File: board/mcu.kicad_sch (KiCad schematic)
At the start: 21 parts, among them J2 PinHeader_01x05, J3 TC2030-MCP-NL, SW1 SW_Push, U1 STM32F030C8Tx, U2 SRV05-4, Y1 16Mhz

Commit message: Update schematic
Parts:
- removed D1: Status, symbol Device:LED_Small
- removed R3: 1k, symbol Device:R_Small
- R301: renamed from R2; value 47 -> 10k
- R303: renamed from R502; value 100R -> 150R
- R304: renamed from R501; value 100R -> 150R
- R305: renamed from R504; value 100R -> 150R
- renumbered C8 to C301, C10 to C302, C9 to C303, C4 to C304, C5 to C305, C6 to C306, C7 to C307, C11 to C308, J3 to J301, J2 to J302, R1 to R302, SW1 to SW301, U1 to U301, U2 to U302, Y1 to Y301
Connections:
- net MCU_BOOT0 renamed OPT_BOOT0
- no-connect marks 1 -> 2
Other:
- note removed: "Status Indicators"
- company: (none) -> BlueDot, Vincenzo Fortunato
- title: (none) -> BD845-PWB

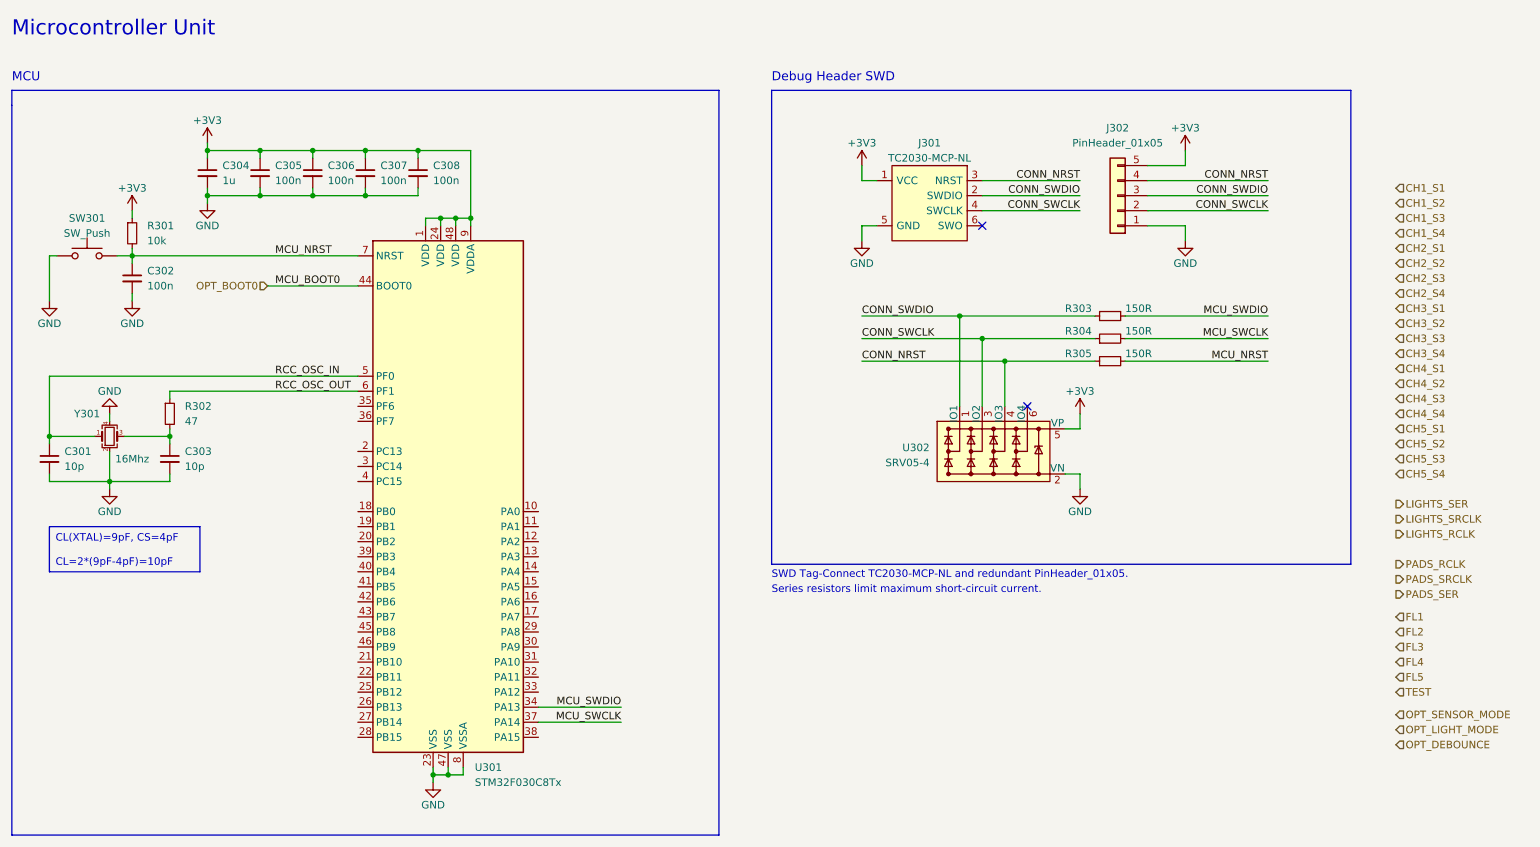
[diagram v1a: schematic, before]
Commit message: Schematic done
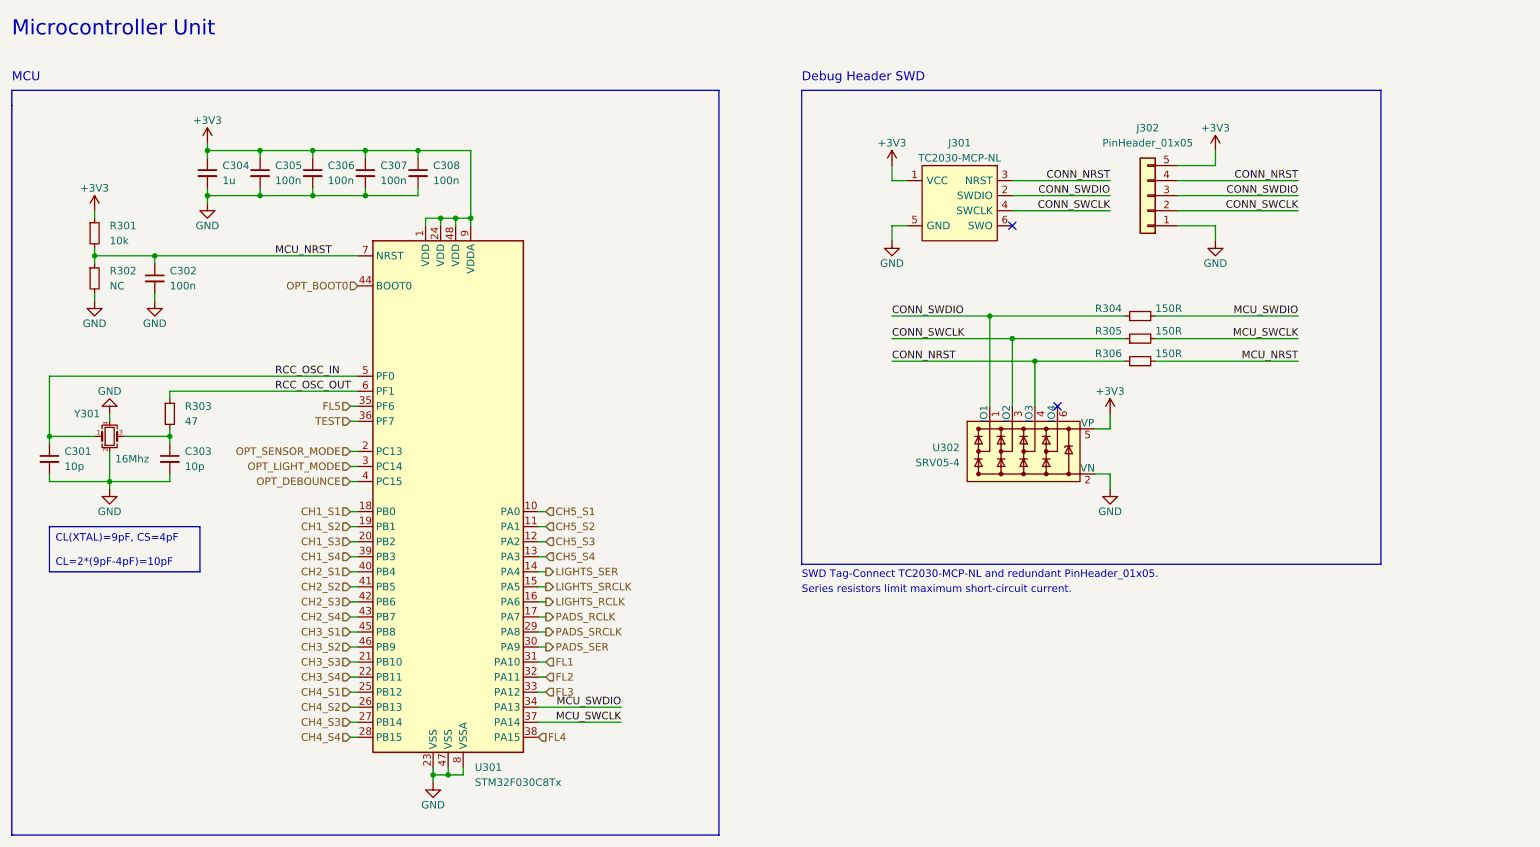
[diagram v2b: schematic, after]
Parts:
- removed SW301: SW_Push, symbol Switch:SW_Push
- added R302: NC, Resistor_SMD:R_0603_1608Metric, symbol Device:R_Small
- C301, C302, C303, C304, C305, C306, C307, C308: footprint (none) -> Capacitor_SMD:C_0603_1608Metric
- J302: footprint (none) -> Connector_PinHeader_2.54mm:PinHeader_1x05_P2.54mm_Vertical
- R301: footprint (none) -> Resistor_SMD:R_0603_1608Metric
- R303: renamed from R302; footprint (none) -> Resistor_SMD:R_0603_1608Metric
- R304: renamed from R303; footprint (none) -> Resistor_SMD:R_0603_1608Metric
- R305: renamed from R304; footprint (none) -> Resistor_SMD:R_0603_1608Metric
- R306: renamed from R305; footprint (none) -> Resistor_SMD:R_0603_1608Metric
- Y301: footprint (none) -> Crystal:Crystal_SMD_3225-4Pin_3.2x2.5mm
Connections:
- net CH1_S1: now also U301.18 (PB0)
- net CH1_S2: now also U301.19 (PB1)
- net CH1_S3: now also U301.20 (PB2)
- net CH1_S4: now also U301.39 (PB3)
- net CH2_S1: now also U301.40 (PB4)
- net CH2_S2: now also U301.41 (PB5)
- net CH2_S3: now also U301.42 (PB6)
- net CH2_S4: now also U301.43 (PB7)
- net CH3_S1: now also U301.45 (PB8)
- net CH3_S2: now also U301.46 (PB9)
- net CH3_S3: now also U301.21 (PB10)
- net CH3_S4: now also U301.22 (PB11)
- net CH4_S1: now also U301.25 (PB12)
- net CH4_S2: now also U301.26 (PB13)
- net CH4_S3: now also U301.27 (PB14)
- net CH4_S4: now also U301.28 (PB15)
- net CH5_S1: now also U301.10 (PA0)
- net CH5_S2: now also U301.11 (PA1)
- net CH5_S3: now also U301.12 (PA2)
- net CH5_S4: now also U301.13 (PA3)
- net FL1: now also U301.31 (PA10)
- net FL2: now also U301.32 (PA11)
- net FL3: now also U301.33 (PA12)
- net FL4: now also U301.38 (PA15)
- net FL5: now also U301.35 (PF6)
- net GND: now also R302.2
- net LIGHTS_RCLK: now also U301.16 (PA6)
- net LIGHTS_SER: now also U301.14 (PA4)
- net LIGHTS_SRCLK: now also U301.15 (PA5)
- net MCU_NRST: now also R302.1
- net OPT_DEBOUNCE: now also U301.4 (PC15)
- net OPT_LIGHT_MODE: now also U301.3 (PC14)
- net OPT_SENSOR_MODE: now also U301.2 (PC13)
- net PADS_RCLK: now also U301.17 (PA7)
- net PADS_SER: now also U301.30 (PA9)
- net PADS_SRCLK: now also U301.29 (PA8)
- net TEST: now also U301.36 (PF7)
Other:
- moved on the sheet: C302, J301, J302, R301, R304, R305, R306, U302

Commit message: Update PCB
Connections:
- net CH1_S1: now also U301.35 (PF6); no longer U301.18 (PB0)
- net CH1_S2: now also U301.33 (PA12); no longer U301.19 (PB1)
- net CH1_S3: now also U301.32 (PA11); no longer U301.20 (PB2)
- net CH1_S4: now also U301.31 (PA10); no longer U301.39 (PB3)
- net CH2_S1: now also U301.30 (PA9); no longer U301.40 (PB4)
- net CH2_S2: now also U301.29 (PA8); no longer U301.41 (PB5)
- net CH2_S3: now also U301.28 (PB15); no longer U301.42 (PB6)
- net CH2_S4: now also U301.27 (PB14); no longer U301.43 (PB7)
- net CH3_S1: now also U301.26 (PB13); no longer U301.45 (PB8)
- net CH3_S2: now also U301.25 (PB12); no longer U301.46 (PB9)
- net CH3_S3: now also U301.22 (PB11); no longer U301.21 (PB10)
- net CH3_S4: now also U301.21 (PB10); no longer U301.22 (PB11)
- net CH4_S1: now also U301.20 (PB2); no longer U301.25 (PB12)
- net CH4_S2: now also U301.19 (PB1); no longer U301.26 (PB13)
- net CH4_S3: now also U301.18 (PB0); no longer U301.27 (PB14)
- net CH4_S4: now also U301.17 (PA7); no longer U301.28 (PB15)
- net CH5_S1: now also U301.16 (PA6); no longer U301.10 (PA0)
- net CH5_S2: now also U301.15 (PA5); no longer U301.11 (PA1)
- net CH5_S3: now also U301.14 (PA4); no longer U301.12 (PA2)
- net FL1: now also U301.46 (PB9); no longer U301.31 (PA10)
- net FL2: now also U301.45 (PB8); no longer U301.32 (PA11)
- net FL3: now also U301.43 (PB7); no longer U301.33 (PA12)
- net FL4: now also U301.42 (PB6); no longer U301.38 (PA15)
- net FL5: now also U301.41 (PB5); no longer U301.35 (PF6)
- net LIGHTS_RCLK: now also U301.11 (PA1); no longer U301.16 (PA6)
- net LIGHTS_SER: now also U301.12 (PA2); no longer U301.14 (PA4)
- net LIGHTS_SRCLK: now also U301.10 (PA0); no longer U301.15 (PA5)
- net OPT_DEBOUNCE: now also U301.38 (PA15); no longer U301.4 (PC15)
- net OPT_LIGHT_MODE: now also U301.36 (PF7); no longer U301.3 (PC14)
- net OPT_SENSOR_MODE: now also U301.39 (PB3); no longer U301.2 (PC13)
- net PADS_RCLK: now also U301.3 (PC14); no longer U301.17 (PA7)
- net PADS_SER: now also U301.2 (PC13); no longer U301.30 (PA9)
- net PADS_SRCLK: now also U301.4 (PC15); no longer U301.29 (PA8)
- net TEST: now also U301.40 (PB4); no longer U301.36 (PF7)

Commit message: Update PCB
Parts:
- C304: value 1u -> 10u
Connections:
- net CONN_NRST: now also R304.1, U302.1 (IO1); no longer R306.1, U302.4 (IO3)
- net CONN_SWDIO: now also R306.1, U302.4 (IO3); no longer R304.1, U302.1 (IO1)
- net MCU_NRST: now also R304.2; no longer R306.2
- net MCU_SWDIO: now also R306.2; no longer R304.2
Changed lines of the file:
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@@
     (effects (font (size 1.27 1.27)) (justify left bottom))
   )
+  (label "CONN_NRST" (at 180.34 72.39 0) (fields_autoplaced)
+    (effects (font (size 1.27 1.27)) (justify left bottom))
+  )
   (label "MCU_SWCLK" (at 142.24 140.97 180) (fields_autoplaced)
     (effects (font (size 1.27 1.27)) (justify right bottom))
-  )
-  (label "CONN_NRST" (at 180.34 80.01 0) (fields_autoplaced)
-    (effects (font (size 1.27 1.27)) (justify left bottom))
   )
   (label "CONN_SWDIO" (at 217.17 52.07 180) (fields_autoplaced)
@@
     (effects (font (size 1.27 1.27)) (justify left bottom))
   )
+  (label "MCU_NRST" (at 248.92 72.39 180) (fields_autoplaced)
+    (effects (font (size 1.27 1.27)) (justify right bottom))
+  )
   (label "CONN_SWCLK" (at 248.92 54.61 180) (fields_autoplaced)
     (effects (font (size 1.27 1.27)) (justify right bottom))
@@
     (effects (font (size 1.27 1.27)) (justify left bottom))
   )
+  (label "MCU_SWDIO" (at 248.92 80.01 180) (fields_autoplaced)
+    (effects (font (size 1.27 1.27)) (justify right bottom))
+  )
   (label "CONN_SWDIO" (at 248.92 52.07 180) (fields_autoplaced)
     (effects (font (size 1.27 1.27)) (justify right bottom))
   )
-  (label "MCU_SWDIO" (at 248.92 72.39 180) (fields_autoplaced)
-    (effects (font (size 1.27 1.27)) (justify right bottom))
-  )
-  (label "MCU_NRST" (at 248.92 80.01 180) (fields_autoplaced)
-    (effects (font (size 1.27 1.27)) (justify right bottom))
-  )
   (label "CONN_NRST" (at 248.92 49.53 180) (fields_autoplaced)
     (effects (font (size 1.27 1.27)) (justify right bottom))
   )
+  (label "CONN_SWDIO" (at 180.34 80.01 0) (fields_autoplaced)
+    (effects (font (size 1.27 1.27)) (justify left bottom))
+  )
   (label "MCU_SWCLK" (at 248.92 76.2 180) (fields_autoplaced)
     (effects (font (size 1.27 1.27)) (justify right bottom))
-  )
-  (label "CONN_SWDIO" (at 180.34 72.39 0) (fields_autoplaced)
-    (effects (font (size 1.27 1.27)) (justify left bottom))
   )
   (label "CONN_SWCLK" (at 217.17 54.61 180) (fields_autoplaced)
@@
     (effects (font (size 1.27 1.27)) (justify right))
   )
+  (hierarchical_label "LIGHTS_SRCLK" (shape output) (at 121.92 105.41 0) (fields_autoplaced)
+    (effects (font (size 1.27 1.27)) (justify left))
+  )
   (hierarchical_label "TEST" (shape input) (at 88.9 115.57 180) (fields_autoplaced)
     (effects (font (size 1.27 1.27)) (justify right))
@@
     (effects (font (size 1.27 1.27)) (justify right))
   )
+  (hierarchical_label "LIGHTS_SER" (shape output) (at 121.92 110.49 0) (fields_autoplaced)
+    (effects (font (size 1.27 1.27)) (justify left))
+  )
   (hierarchical_label "CH4_S3" (shape input) (at 88.9 105.41 180) (fields_autoplaced)
     (effects (font (size 1.27 1.27)) (justify right))
@@
     (effects (font (size 1.27 1.27)) (justify right))
   )
-  (hierarchical_label "LIGHTS_SRCLK" (shape output) (at 121.92 105.41 0) (fields_autoplaced)
-    (effects (font (size 1.27 1.27)) (justify left))
-  )
   (hierarchical_label "OPT_BOOT0" (shape input) (at 88.9 67.31 180) (fields_autoplaced)
     (effects (font (size 1.27 1.27)) (justify right))
@@
   (hierarchical_label "CH3_S3" (shape input) (at 88.9 133.35 180) (fields_autoplaced)
     (effects (font (size 1.27 1.27)) (justify right))
-  )
-  (hierarchical_label "LIGHTS_SER" (shape output) (at 121.92 110.49 0) (fields_autoplaced)
-    (effects (font (size 1.27 1.27)) (justify left))
   )
   (hierarchical_label "CH4_S4" (shape input) (at 121.92 123.19 0) (fields_autoplaced)
@@
       (effects (font (size 1.27 1.27)) (justify left))
     )
-    (property "Value" "1u" (at 67.31 49.53 0)
+    (property "Value" "10u" (at 67.31 49.53 0)
       (effects (font (size 1.27 1.27)) (justify left))
     )
@@
       (project "bd845-pwb"
         (path "/c0443f53-6229-4858-b0f1-180b8ed8e6c2/1c1d22e9-ff5a-4d59-8d81-13b47946e5d6"
-          (reference "C304") (unit 1) (value "1u") (footprint "Capacitor_SMD:C_0603_1608Metric")
-        )
-      )
+          (reference "C304") (unit 1) (value "10u") (footprint "Capacitor_SMD:C_0603_1608Metric")
+        )
+      )

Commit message: Update PCB
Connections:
- net OPT_LIGHT_MODE renamed OPT_LIGHT
- net OPT_SENSOR_MODE renamed OPT_LEGACY
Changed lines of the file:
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@@
     (effects (font (size 1.27 1.27)) (justify right))
   )
-  (hierarchical_label "OPT_SENSOR_MODE" (shape input) (at 88.9 113.03 180) (fields_autoplaced)
+  (hierarchical_label "OPT_LEGACY" (shape input) (at 88.9 113.03 180) (fields_autoplaced)
     (effects (font (size 1.27 1.27)) (justify right))
   )
@@
     (effects (font (size 1.27 1.27)) (justify right))
   )
-  (hierarchical_label "OPT_LIGHT_MODE" (shape input) (at 88.9 90.17 180) (fields_autoplaced)
+  (hierarchical_label "OPT_LIGHT" (shape input) (at 88.9 90.17 180) (fields_autoplaced)
     (effects (font (size 1.27 1.27)) (justify right))
   )

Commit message: Select input TVS diode
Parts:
- R303: value 47 -> 47R
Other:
- title: BD845-PWB -> BD845-PWB SCH
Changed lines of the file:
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@@
   (paper "A4")
   (title_block
-    (title "BD845-PWB")
+    (title "BD845-PWB SCH")
     (date "2022-11-27")
-    (rev "1")
+    (rev "1.0.0")
     (company "BlueDot, Vincenzo Fortunato")
   )
@@
       (effects (font (size 1.27 1.27)) (justify left))
     )
-    (property "Value" "47" (at 60.96 90.17 0)
+    (property "Value" "47R" (at 60.96 90.17 0)
       (effects (font (size 1.27 1.27)) (justify left))
     )
@@
       (project "bd845-pwb"
         (path "/c0443f53-6229-4858-b0f1-180b8ed8e6c2/1c1d22e9-ff5a-4d59-8d81-13b47946e5d6"
-          (reference "R303") (unit 1) (value "47") (footprint "Resistor_SMD:R_0603_1608Metric")
-        )
-      )
+          (reference "R303") (unit 1) (value "47R") (footprint "Resistor_SMD:R_0603_1608Metric")
+        )
+      )
